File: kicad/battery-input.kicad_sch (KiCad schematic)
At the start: 8 parts, among them J1 KF7620-7.62-2P, Q1 SP40P04NK

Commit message: IPC footprint renaming, battery sim added
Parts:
- D1, D3: footprint MyParts:SMC_L6.9-W5.9-LS7.9-RD -> MyPartsIPC:DIOM7959X262N
- D2: footprint MyParts:SOD-123_L2.7-W1.6-LS3.7-RD -> MyPartsIPC:SOD3716X135N
- Q1: footprint MyParts:PDFN-8_L6.0-W5.0-P1.27_HGQ065NE4A -> MyPartsIPC:SON127P600X500X110-9N
- R1: footprint MyParts:R0402 -> MyPartsIPC:RESC1005X40N
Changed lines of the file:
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@@
 			)
 		)
-		(property "Footprint" "MyParts:SMC_L6.9-W5.9-LS7.9-RD"
+		(property "Footprint" "MyPartsIPC:DIOM7959X262N"
 			(at 175.26 71.12 0)
 			(hide yes)
@@
 			)
 		)
-		(property "Footprint" "MyParts:R0402"
+		(property "Footprint" "MyPartsIPC:RESC1005X40N"
 			(at 137.16 88.9 0)
 			(hide yes)
@@
 			)
 		)
-		(property "Footprint" "MyParts:SOD-123_L2.7-W1.6-LS3.7-RD"
+		(property "Footprint" "MyPartsIPC:SOD3716X135N"
 			(at 139.7 80.01 0)
 			(hide yes)
@@
 			)
 		)
-		(property "Footprint" "MyParts:PDFN-8_L6.0-W5.0-P1.27_HGQ065NE4A"
+		(property "Footprint" "MyPartsIPC:SON127P600X500X110-9N"
 			(at 129.54 74.93 0)
 			(hide yes)
@@
 			)
 		)
-		(property "Footprint" "MyParts:SMC_L6.9-W5.9-LS7.9-RD"
+		(property "Footprint" "MyPartsIPC:DIOM7959X262N"
 			(at 161.29 78.74 0)
 			(hide yes)
@@
 				)
 			)
+		)
+	)
+	(netclass_flag ""
+		(length 2.54)
+		(shape round)
+		(at 156.21 72.39 180)
+		(effects
+			(font
+				(size 1.27 1.27)
+			)
+			(justify right top)
+		)
+		(property "Net Class" "V_BAT"
+			(at 157.48 76.2 0)
+			(show_name no)
+			(do_not_autoplace no)
+			(effects
+				(font
+					(size 1.27 1.27)
+					(italic yes)
+				)
+				(justify left)
+			)
+		)
+		(property "VOLTAGE_NOM" "12.8V"
+			(at 157.48 76.2 0)
+			(hide yes)
+			(show_name no)
+			(do_not_autoplace no)
+			(effects
+				(font
+					(size 1.27 1.27)
+				)
+			)
+		)
+		(property "VOLTAGE_MIN" "10.0V"
+			(at 157.48 76.2 0)
+			(hide yes)
+			(show_name no)
+			(do_not_autoplace no)
+			(effects
+				(font
+					(size 1.27 1.27)
+				)
+			)
+		)
+		(property "VOLTAGE_MAX" "14.6V"
+			(at 157.48 76.2 0)
+			(hide yes)
+			(show_name no)
+			(do_not_autoplace no)
+			(effects
+				(font
+					(size 1.27 1.27)
+				)
+			)
+		)
+		(property "VOLTAGE_EXCURSION_MAX" "18.0V"
+			(at 157.48 76.2 0)
+			(hide yes)
+			(show_name no)
+			(do_not_autoplace no)
+			(effects
+				(font
+					(size 1.27 1.27)
+				)
+			)

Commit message: Updates after latest Tomachie review
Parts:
- F1, F2: Fuse Type (none) -> Fast-acting ATO (Littelfuse 287 series); Interrupting Rating (none) -> 1000A @ 32VDC; Voltage Rating (none) -> 32VDC
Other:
- note added: "F1/F2 are the backup for a reversed battery: they blow only if Q1 has failed short (about 270 A then flows through D1/D3 and the RoboClaw diodes). Check polarity and Q1 before replacing a blown fuse."
- note added: "Standby drain: SW1 (power sheet) switches the CM4 / logic supply only. With SW1 off the battery still feeds the RoboClaw logic (~30 mA, via F1) and U11 + dividers (~1.3 mA): about 31 mA, so 12 Ah lasts ~16 days. For storage or transport unplug J1 (or remove F1/F2); charge first."
- note removed: "Designed to survive battery connected reverse. Fuses may blow, but are cheap an easy to replace."
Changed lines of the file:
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@@
+		)
+	)
+	(text "Standby drain: SW1 (power sheet) switches the CM4 / logic supply only.\nWith SW1 off the battery still feeds the RoboClaw logic (~30 mA, via F1)\nand U11 + dividers (~1.3 mA): about 31 mA, so 12 Ah lasts ~16 days.\nFor storage or transport unplug J1 (or remove F1/F2); charge first."
+		(exclude_from_sim no)
+		(at 107.95 142.24 0)
+		(effects
+			(font
+				(size 1.27 1.27)
+			)
+			(justify left top)
 		)
 	)
@@
 		)
 	)
-	(text "Designed to survive battery connected reverse.\nFuses may blow, but are cheap an easy to replace."
+	(text "F1/F2 are the backup for a reversed battery: they blow only if Q1\nhas failed short (about 270 A then flows through D1/D3 and the RoboClaw\ndiodes). Check polarity and Q1 before replacing a blown fuse."
 		(exclude_from_sim no)
 		(at 107.95 134.366 0)
 		(effects
 			(font
-				(size 1.524 1.524)
+				(size 1.27 1.27)
 			)
 			(justify left)
@@
 	(wire
 		(pts
-			(xy 167.64 66.04) (xy 170.18 66.04)
-		)
-		(stroke
-			(width 0)
-			(type default)
-		)
-	)
-	(wire
-		(pts
 			(xy 142.24 66.04) (xy 143.51 66.04)
 		)
@@
 		(pts
 			(xy 157.48 72.39) (xy 153.67 72.39)
+		)
+		(stroke
+			(width 0)
+			(type default)
+		)
+	)
+	(wire
+		(pts
+			(xy 167.64 66.04) (xy 175.26 66.04)
 		)
 		(stroke
@@
 	(hierarchical_label "V_MOTOR"
 		(shape output)
-		(at 170.18 66.04 0)
+		(at 175.26 66.04 0)
 		(effects
 			(font
@@
 			)
 			(justify left)
+		)
+	)
+	(netclass_flag ""
+		(length 2.54)
+		(shape round)
+		(at 172.72 66.04 0)
+		(effects
+			(font
+				(size 1.27 1.27)
+			)
+			(justify left bottom)
+		)
+		(property "Net Class" "V_MOTOR"
+			(at 173.99 62.23 0)
+			(show_name no)
+			(do_not_autoplace no)
+			(effects
+				(font
+					(size 1.27 1.27)
+					(italic yes)
+				)
+				(justify left)
+			)
+		)
+		(property "VOLTAGE_NOM" "12.8V"
+			(at 173.99 62.23 0)
+			(hide yes)
+			(show_name no)
+			(do_not_autoplace no)
+			(effects
+				(font
+					(size 1.27 1.27)
+				)
+			)
+		)
+		(property "VOLTAGE_MIN" "10.0V"
+			(at 173.99 62.23 0)
+			(hide yes)
+			(show_name no)
+			(do_not_autoplace no)
+			(effects
+				(font
+					(size 1.27 1.27)
+				)
+			)
+		)
+		(property "VOLTAGE_MAX" "14.6V"
+			(at 173.99 62.23 0)
+			(hide yes)
+			(show_name no)
+			(do_not_autoplace no)
+			(effects
+				(font
+					(size 1.27 1.27)
+				)
+			)
+		)
+		(property "VOLTAGE_EXCURSION_MAX" "22V"
+			(at 173.99 62.23 0)
+			(hide yes)
+			(show_name no)
+			(do_not_autoplace no)
+			(effects
+				(font
+					(size 1.27 1.27)
+				)
+			)
+		)
+	)
+	(netclass_flag ""
+		(length 2.54)
+		(shape round)
+		(at 156.21 72.39 180)
+		(effects
+			(font
+				(size 1.27 1.27)
+			)
+			(justify right top)
+		)
+		(property "Net Class" "V_BAT"
+			(at 157.48 76.2 0)
+			(show_name no)
+			(do_not_autoplace no)
+			(effects
+				(font
+					(size 1.27 1.27)
+					(italic yes)
+				)
+				(justify left)
+			)
+		)
+		(property "VOLTAGE_NOM" "12.8V"
+			(at 157.48 76.2 0)
+			(hide yes)
+			(show_name no)
+			(do_not_autoplace no)
+			(effects
+				(font
+					(size 1.27 1.27)
+				)
+			)
+		)
+		(property "VOLTAGE_MIN" "10.0V"
+			(at 157.48 76.2 0)
+			(hide yes)
+			(show_name no)
+			(do_not_autoplace no)
+			(effects
+				(font
+					(size 1.27 1.27)
+				)
+			)
+		)
+		(property "VOLTAGE_MAX" "14.6V"
+			(at 157.48 76.2 0)
+			(hide yes)
+			(show_name no)
+			(do_not_autoplace no)
+			(effects
+				(font
+					(size 1.27 1.27)
+				)
+			)
+		)
+		(property "VOLTAGE_EXCURSION_MAX" "22V"
+			(at 157.48 76.2 0)
+			(hide yes)
+			(show_name no)
+			(do_not_autoplace no)
+			(effects
+				(font
+					(size 1.27 1.27)
+				)
+			)
 		)
 	)
@@
 			)
 		)
+		(property "Voltage Rating" "32VDC"
+			(at 148.59 66.04 0)
+			(hide yes)
+			(show_name no)
+			(do_not_autoplace no)
+			(effects
+				(font
+					(size 1.27 1.27)
+				)
+			)
+		)
+		(property "Interrupting Rating" "1000A @ 32VDC"
+			(at 148.59 66.04 0)
+			(hide yes)
+			(show_name no)
+			(do_not_autoplace no)
+			(effects
+				(font
+					(size 1.27 1.27)
+				)
+			)
+		)
+		(property "Fuse Type" "Fast-acting ATO (Littelfuse 287 series)"
+			(at 148.59 66.04 0)
+			(hide yes)
+			(show_name no)
+			(do_not_autoplace no)
+			(effects
+				(font
+					(size 1.27 1.27)
+				)
+			)
+		)
 		(pin "1"
 		)
@@
 			)
 		)
+		(property "Voltage Rating" "32VDC"
+			(at 148.59 72.39 0)
+			(hide yes)
+			(show_name no)
+			(do_not_autoplace no)
+			(effects
+				(font
+					(size 1.27 1.27)
+				)
+			)
+		)
+		(property "Interrupting Rating" "1000A @ 32VDC"
+			(at 148.59 72.39 0)
+			(hide yes)
+			(show_name no)
+			(do_not_autoplace no)
+			(effects
+				(font
+					(size 1.27 1.27)
+				)
+			)
+		)
+		(property "Fuse Type" "Fast-acting ATO (Littelfuse 287 series)"
+			(at 148.59 72.39 0)
+			(hide yes)
+			(show_name no)
+			(do_not_autoplace no)
+			(effects
+				(font
+					(size 1.27 1.27)
+				)
+			)
+		)
 		(pin "1"
 		)
@@
 				)
 			)
-		)
-	)
-	(netclass_flag ""
-		(length 2.54)
-		(shape round)
-		(at 156.21 72.39 180)
-		(effects
-			(font
-				(size 1.27 1.27)
-			)
-			(justify right top)
-		)
-		(property "Net Class" "V_BAT"
-			(at 157.48 76.2 0)
-			(show_name no)
-			(do_not_autoplace no)
-			(effects
-				(font
-					(size 1.27 1.27)
-					(italic yes)
-				)
-				(justify left)
-			)
-		)
-		(property "VOLTAGE_NOM" "12.8V"
-			(at 157.48 76.2 0)
-			(hide yes)
-			(show_name no)
-			(do_not_autoplace no)
-			(effects
-				(font
-					(size 1.27 1.27)
-				)
-			)
-		)
-		(property "VOLTAGE_MIN" "10.0V"
-			(at 157.48 76.2 0)
-			(hide yes)
-			(show_name no)
-			(do_not_autoplace no)
-			(effects
-				(font
-					(size 1.27 1.27)
-				)
-			)
-		)
-		(property "VOLTAGE_MAX" "14.6V"
-			(at 157.48 76.2 0)
-			(hide yes)
-			(show_name no)
-			(do_not_autoplace no)
-			(effects
-				(font
-					(size 1.27 1.27)
-				)
-			)
-		)
-		(property "VOLTAGE_EXCURSION_MAX" "18.0V"
-			(at 157.48 76.2 0)
-			(hide yes)
-			(show_name no)
-			(do_not_autoplace no)
-			(effects
-				(font
-					(size 1.27 1.27)
-				)
-			)

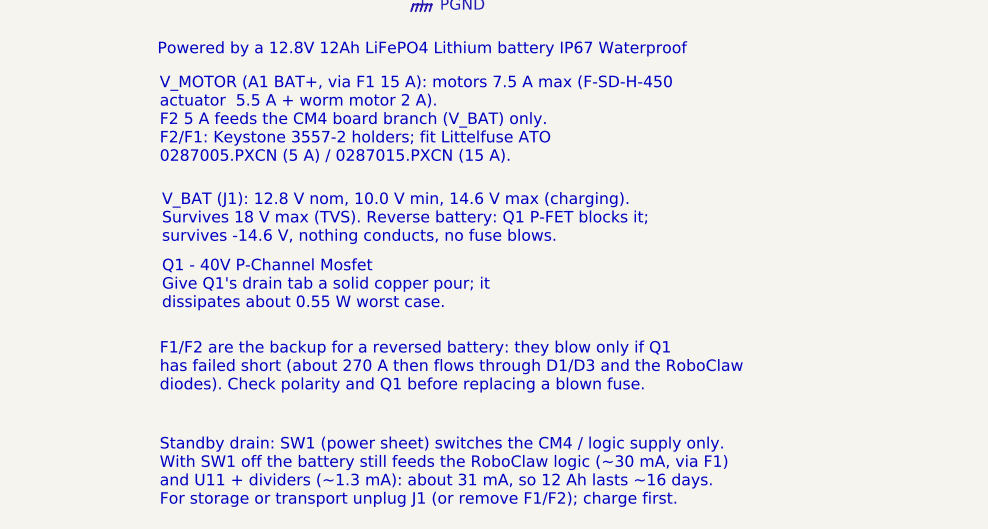
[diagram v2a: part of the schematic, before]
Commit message: Added I2C and battery 3d file
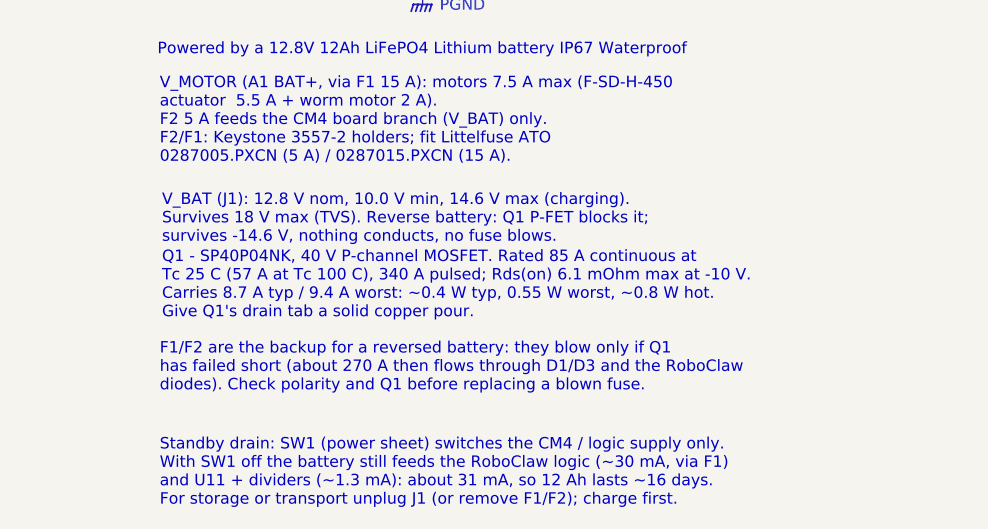
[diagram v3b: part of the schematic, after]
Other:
- note added: "Q1 - SP40P04NK, 40 V P-channel MOSFET. Rated 85 A continuous at Tc 25 C (57 A at Tc 100 C), 340 A pulsed; Rds(on) 6.1 mOhm max at -10 V. Carries 8.7 A typ / 9.4 A worst: ~0.4 W typ, 0.55 W worst, ~0.8 W hot. Give Q1's drain tab a solid copper pour."
- note removed: "Q1 - 40V P-Channel Mosfet Give Q1's drain tab a solid copper pour; it dissipates about 0.55 W worst case."
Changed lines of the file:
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@@
 		)
 	)
-	(text "Q1 - 40V P-Channel Mosfet\nGive Q1's drain tab a solid copper pour; it \ndissipates about 0.55 W worst case."
+	(text "Q1 - SP40P04NK, 40 V P-channel MOSFET. Rated 85 A continuous at\nTc 25 C (57 A at Tc 100 C), 340 A pulsed; Rds(on) 6.1 mOhm max at -10 V.\nCarries 8.7 A typ / 9.4 A worst: ~0.4 W typ, 0.55 W worst, ~0.8 W hot.\nGive Q1's drain tab a solid copper pour."
 		(exclude_from_sim no)
 		(at 108.204 125.222 0)
